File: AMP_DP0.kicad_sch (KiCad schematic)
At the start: 0 parts

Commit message: Schem upd
added Copressor module
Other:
- added sheet Compression block (Cp.kicad_sch)
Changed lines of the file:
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@@
 	(generator_version "10.0")
 	(paper "A4")
+	(sheet
+		(at 248.92 15.24)
+		(size 35.56 38.1)
+		(exclude_from_sim no)
+		(in_bom yes)
+		(on_board yes)
+		(dnp no)
+		(fields_autoplaced yes)
+		(stroke
+			(width 0.1524)
+			(type solid)
+		)
+		(fill
+			(color 0 0 0 0)
+		)
+		(property "Sheetname" "Compression block"
+			(at 248.92 14.5284 0)
+			(show_name no)
+			(do_not_autoplace no)
+			(effects
+				(font
+					(size 1.27 1.27)
+				)
+				(justify left bottom)
+			)
+		)
+		(property "Sheetfile" "Cp.kicad_sch"
+			(at 248.92 53.9246 0)
+			(show_name no)
+			(do_not_autoplace no)
+			(effects
+				(font
+					(size 1.27 1.27)
+				)
+				(justify left top)
+			)
+		)
+		(instances
+			(project "AMP_DP0"
+				(path "/4094031b-a9da-4ac5-aaa1-42b342c92a3e"
+					(page "2")
+				)
+			)
+		)
+	)
 	(sheet_instances
 		(path "/"

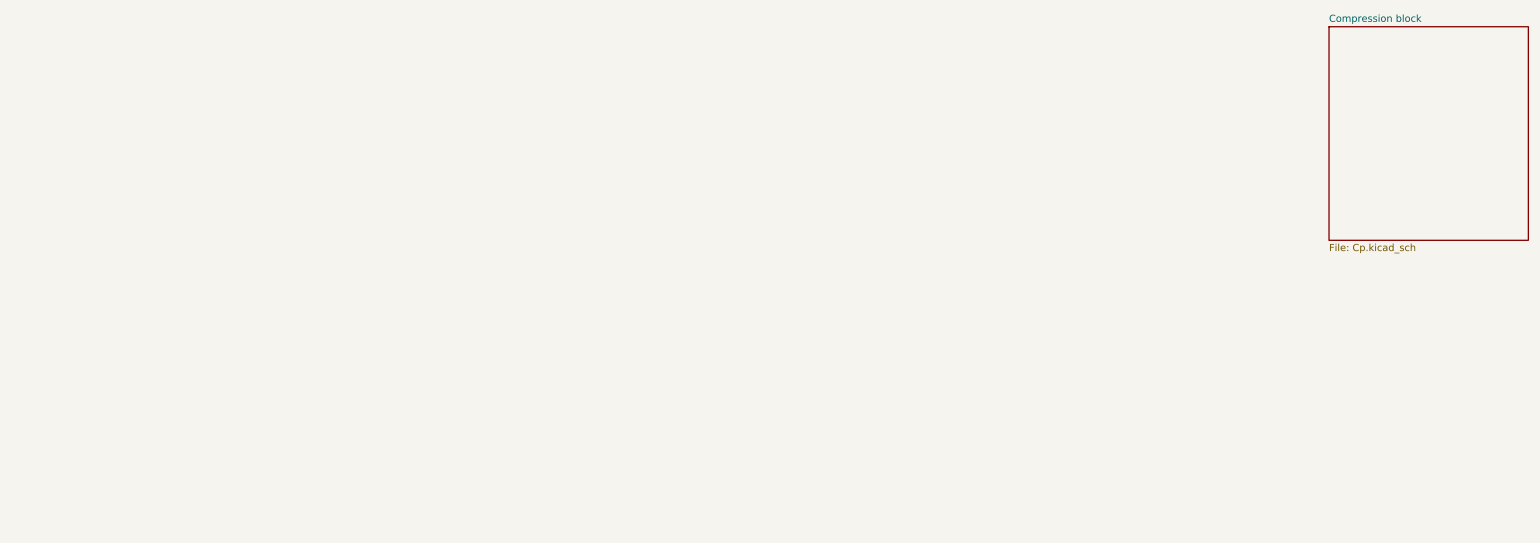
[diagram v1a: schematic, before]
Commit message: Schem upd
added Voltage supply
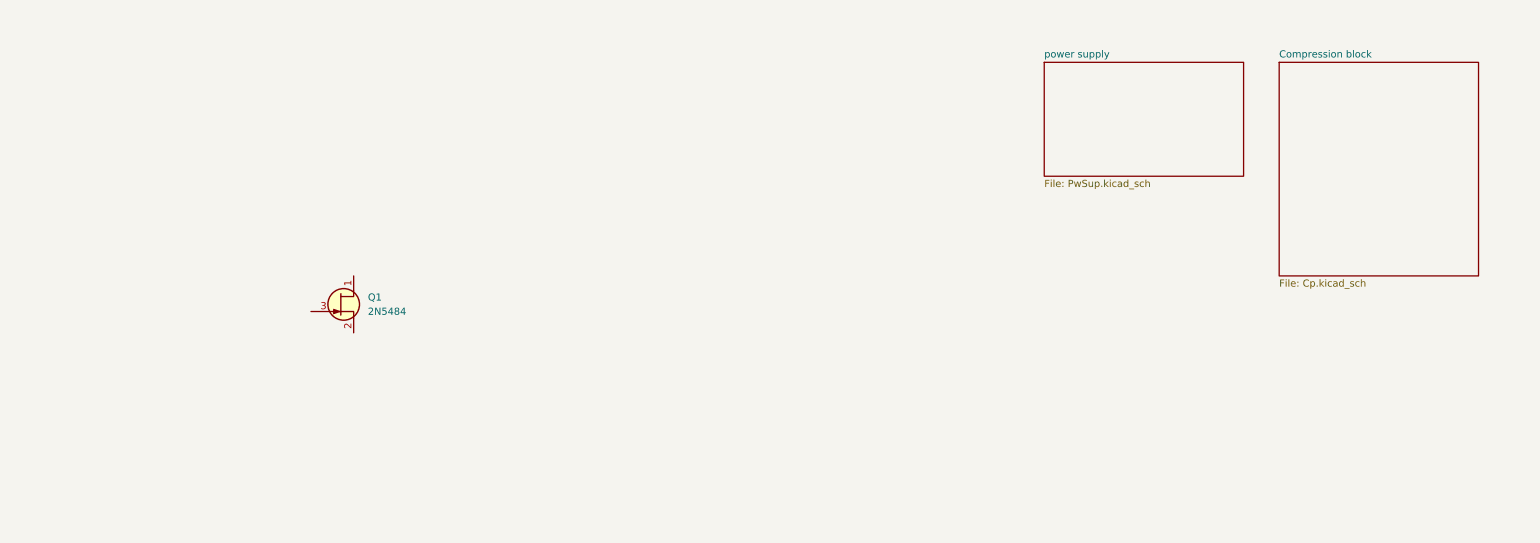
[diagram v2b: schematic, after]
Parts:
- added Q1: 2N5484, PCM_Package_TO_SOT_THT_AKL:TO-92_Inline_Wide_DSG, symbol PCM_Transistor_JFET_AKL:2N5484
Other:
- added sheet power supply (PwSup.kicad_sch)
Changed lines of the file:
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@@
 	(generator_version "10.0")
 	(paper "A4")
+	(symbol
+		(lib_id "PCM_Transistor_JFET_AKL:2N5484")
+		(at 72.39 64.77 0)
+		(unit 1)
+		(body_style 1)
+		(exclude_from_sim no)
+		(in_bom yes)
+		(on_board yes)
+		(in_pos_files yes)
+		(dnp no)
+		(fields_autoplaced yes)
+		(property "Reference" "Q1"
+			(at 77.47 63.4999 0)
+			(show_name no)
+			(do_not_autoplace no)
+			(effects
+				(font
+					(size 1.27 1.27)
+				)
+				(justify left)
+			)
+		)
+		(property "Value" "2N5484"
+			(at 77.47 66.0399 0)
+			(show_name no)
+			(do_not_autoplace no)
+			(effects
+				(font
+					(size 1.27 1.27)
+				)
+				(justify left)
+			)
+		)
+		(property "Footprint" "PCM_Package_TO_SOT_THT_AKL:TO-92_Inline_Wide_DSG"
+			(at 77.47 62.23 0)
+			(hide yes)
+			(show_name no)
+			(do_not_autoplace no)
+			(effects
+				(font
+					(size 1.27 1.27)
+				)
+			)
+		)
+		(property "Datasheet" "https://my.centralsemi.com/datasheets/2N5484-5486.PDF"
+			(at 72.39 66.04 0)
+			(hide yes)
+			(show_name no)
+			(do_not_autoplace no)
+			(effects
+				(font
+					(size 1.27 1.27)
+				)
+			)
+		)
+		(property "Description" "TO-92 N-JFET transistor, 25V, 1mA, 310mW, Alternate KiCAD Library"
+			(at 72.39 64.77 0)
+			(hide yes)
+			(show_name no)
+			(do_not_autoplace no)
+			(effects
+				(font
+					(size 1.27 1.27)
+				)
+			)
+		)
+		(pin "3"
+		)
+		(pin "1"
+		)
+		(pin "2"
+		)
+		(instances
+			(project "AMP_DP0"
+				(path "/4094031b-a9da-4ac5-aaa1-42b342c92a3e"
+					(reference "Q1")
+					(unit 1)
+				)
+			)
+		)
+	)
 	(sheet
-		(at 248.92 15.24)
+		(at 198.12 21.59)
+		(size 35.56 20.32)
+		(exclude_from_sim no)
+		(in_bom yes)
+		(on_board yes)
+		(dnp no)
+		(fields_autoplaced yes)
+		(stroke
+			(width 0.1524)
+			(type solid)
+		)
+		(fill
+			(color 0 0 0 0)
+		)
+		(property "Sheetname" "power supply"
+			(at 198.12 20.8784 0)
+			(show_name no)
+			(do_not_autoplace no)
+			(effects
+				(font
+					(size 1.27 1.27)
+				)
+				(justify left bottom)
+			)
+		)
+		(property "Sheetfile" "PwSup.kicad_sch"
+			(at 198.12 42.4946 0)
+			(show_name no)
+			(do_not_autoplace no)
+			(effects
+				(font
+					(size 1.27 1.27)
+				)
+				(justify left top)
+			)
+		)
+		(instances
+			(project "AMP_DP0"
+				(path "/4094031b-a9da-4ac5-aaa1-42b342c92a3e"
+					(page "3")
+				)
+			)
+		)
+	)
+	(sheet
+		(at 240.03 21.59)
 		(size 35.56 38.1)
 		(exclude_from_sim no)
@@
 		)
 		(property "Sheetname" "Compression block"
-			(at 248.92 14.5284 0)
+			(at 240.03 20.8784 0)
 			(show_name no)
 			(do_not_autoplace no)
@@
 		)
 		(property "Sheetfile" "Cp.kicad_sch"
-			(at 248.92 53.9246 0)
+			(at 240.03 60.2746 0)
 			(show_name no)
 			(do_not_autoplace no)

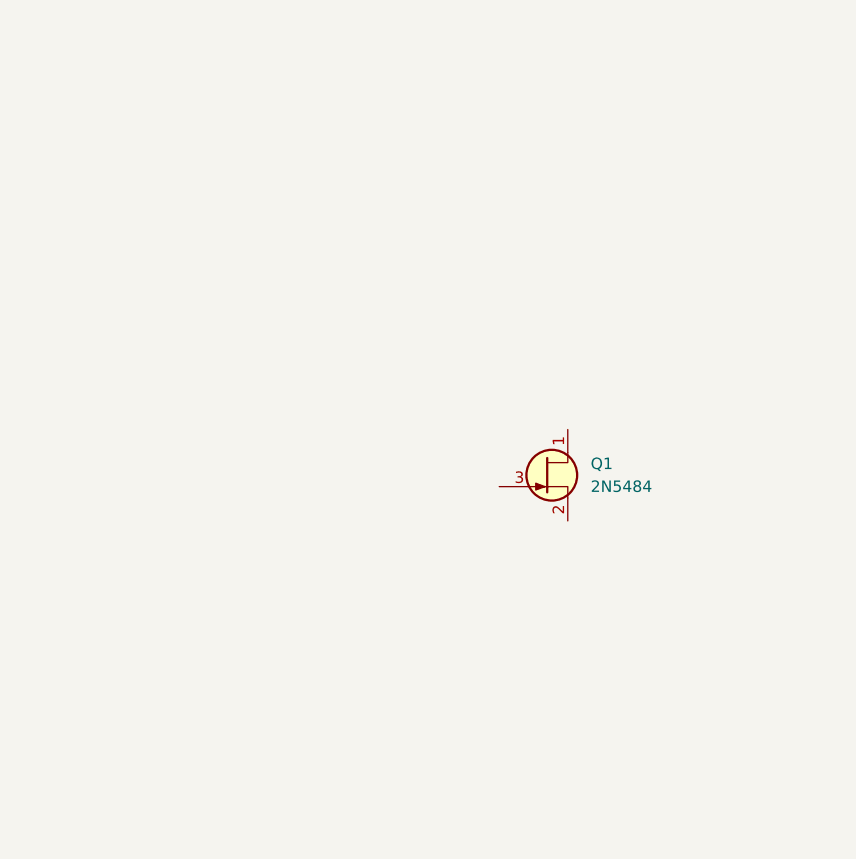
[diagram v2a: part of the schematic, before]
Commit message: Schem & lib upd
added audiojack symbol & added PREAMP cascade
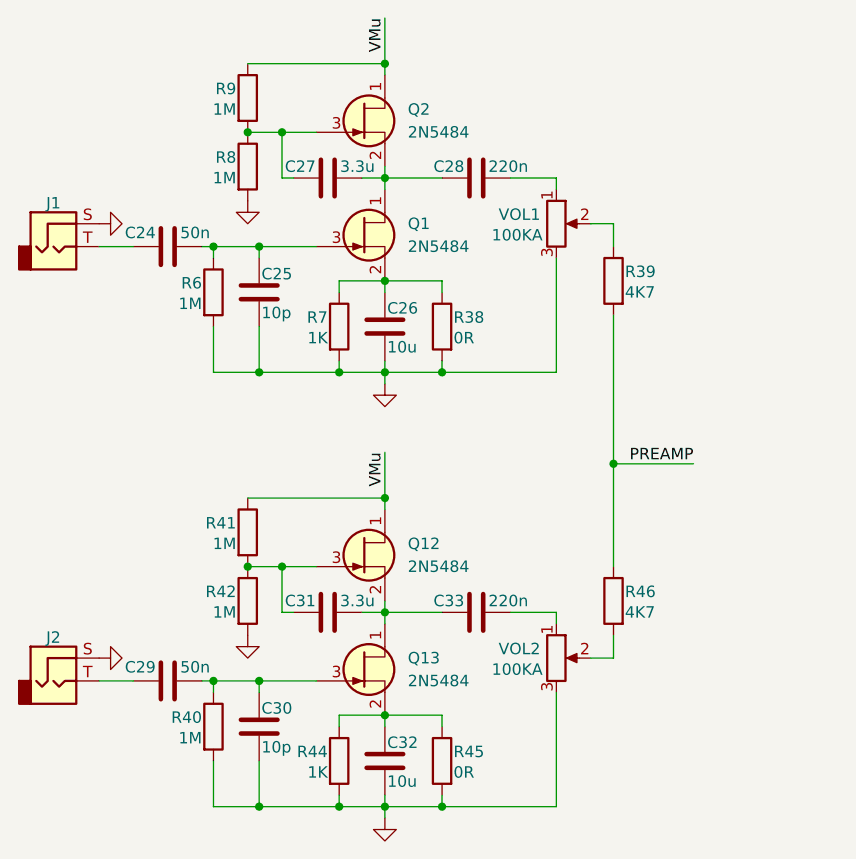
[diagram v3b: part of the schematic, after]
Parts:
- added C24, C29: 50n, symbol Device:C
- added C25, C30: 10p, symbol Device:C
- added C26, C32: 10u, symbol Device:C
- added C27, C31: 3.3u, symbol Device:C
- added C28, C33: 220n, symbol Device:C
- added J1, J2: (no value), symbol PrLib:Audio_Jack
- added Q1, Q12, Q13: 2N5484, PCM_Package_TO_SOT_THT_AKL:TO-92_Inline_Wide_DSG, symbol PCM_Transistor_JFET_AKL:2N5484
- added R38, R45: 0R, symbol Device:R
- added R39, R46: 4K7, symbol Device:R
- added R40, R41, R42, R6, R8, R9: 1M, symbol Device:R
- added R44, R7: 1K, symbol Device:R
- added VOL1, VOL2: 100KA, symbol Device:R_Potentiometer
- renumbered Q1 to Q2
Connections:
- net VMu: now reaches Q2.1 (D)
- net VMu: now also Q12.1 (D), R41.1, R9.1
- net at Q2.2 (S): now also C27.2, C28.1, Q1.1 (D)
- net at Q2.3 (G): now also C27.1, R8.1, R9.2
- new net: C28.2, VOL1.1
- new net: R39.1, VOL1.2
- new net: R46.2, VOL2.2
- new net: C29.1, J2.T
- new net: C29.2, C30.2, Q13.3 (G), R40.1
- new net: C24.2, C25.2, Q1.3 (G), R6.1
- new net: C31.2, C33.1, Q12.2 (S), Q13.1 (D)
- new net: C32.2, Q13.2 (S), R44.1, R45.1
- new net: C24.1, J1.T
- new net: C33.2, VOL2.1
- new net: C26.2, Q1.2 (S), R38.1, R7.1
- new net: C31.1, Q12.3 (G), R41.2, R42.1
- new net GND: C25.1, C26.1, C30.1, C32.1, J1.S, J2.S, R38.2, R40.2, R42.2, R44.2, R45.2, R6.2, R7.2, R8.2, VOL1.3, VOL2.3
- new net PREAMP: R39.2, R46.1
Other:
- moved on the sheet: Q2
